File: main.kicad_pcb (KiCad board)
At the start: 2 copper layers, 221.6 x 89.6 mm, 122 parts, among them SW1 Kailh-Choc, SW10 Kailh-Choc, SW11 Kailh-Choc, SW12 Kailh-Choc, SW13 Kailh-Choc, SW14 Kailh-Choc, SW15 Kailh-Choc, SW16 Kailh-Choc, SW17 Kailh-Choc, SW18 Kailh-Choc, SW19 Kailh-Choc, SW2 Kailh-Choc, SW20 Kailh-Choc, SW21 Kailh-Choc, SW22 Kailh-Choc, SW23 Kailh-Choc, SW24 Kailh-Choc, SW25 Kailh-Choc, SW26 Kailh-Choc, SW27 Kailh-Choc, SW28 Kailh-Choc, SW29 Kailh-Choc, SW3 Kailh-Choc, SW30 Kailh-Choc, SW31 Kailh-Choc, SW32 Kailh-Choc, SW33 Kailh-Choc, SW34 Kailh-Choc, SW4 Kailh-Choc, SW5 Kailh-Choc, SW6 Kailh-Choc, SW7 Kailh-Choc, SW8 Kailh-Choc, SW9 Kailh-Choc, U1 nice_nano, U2 nice_nano

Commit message: Update PCB silk
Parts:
- removed kibuzzard-6361C7AA: G***, kibuzzard-6361C7AA
- added kibuzzard-63703FC3: G***, kibuzzard-63703FC3, B.Cu at (84.8, 87.8)

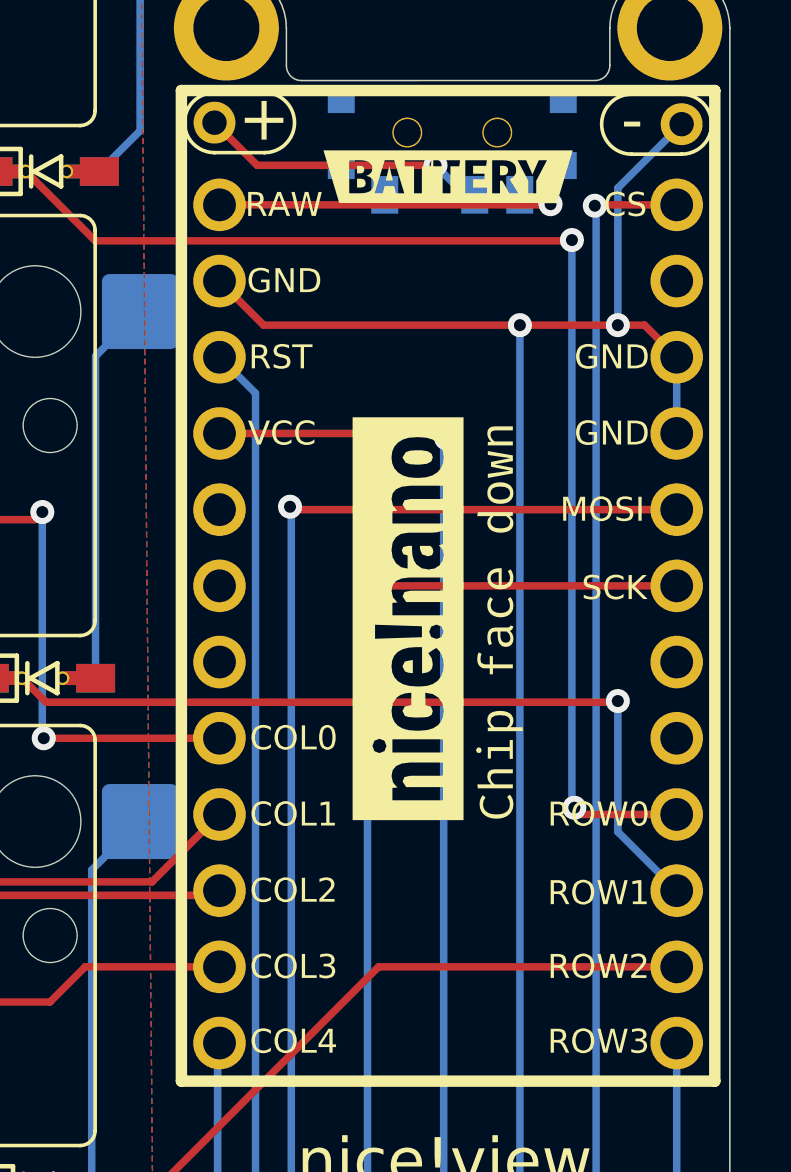
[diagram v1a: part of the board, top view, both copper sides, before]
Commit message: Use local library only
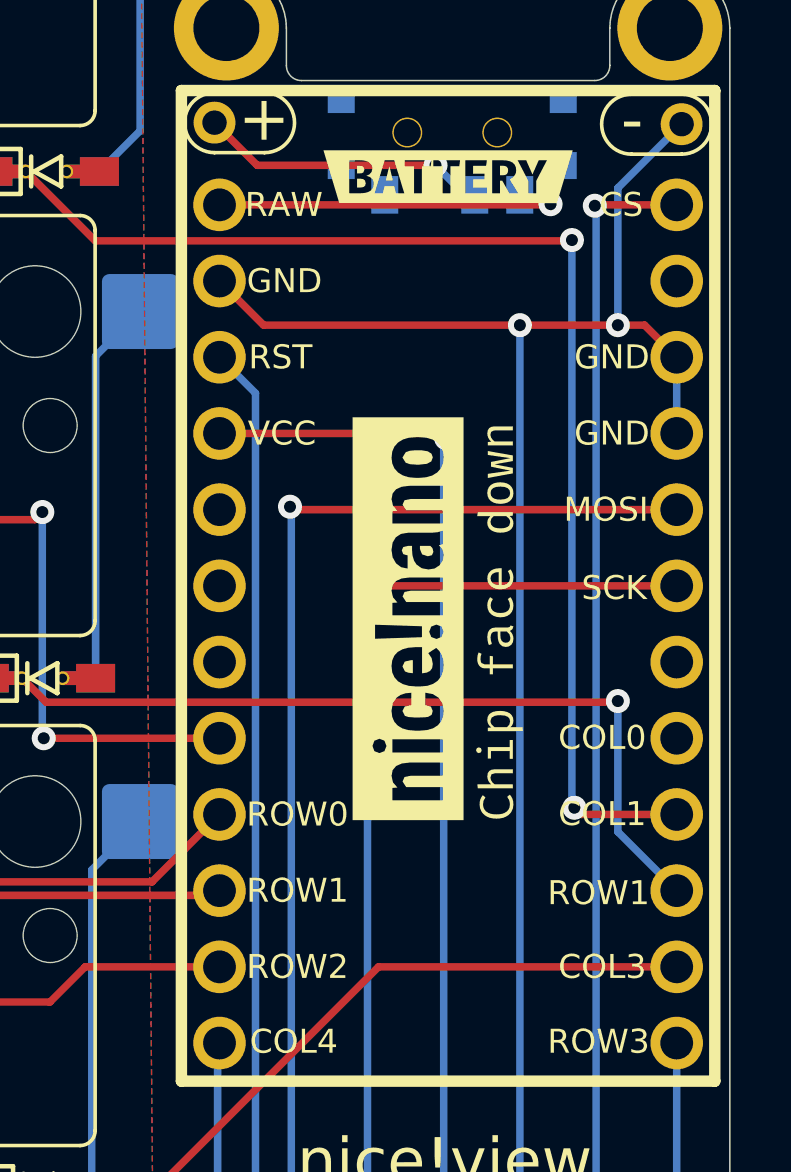
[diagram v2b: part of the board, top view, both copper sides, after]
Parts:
- Bat+0, Bat+1, BatGND0, BatGND1: footprint * duckyb-collection:1pin_Battery -> urchin-footprints:1pin_Battery
- D1, D10, D11, D12, D13, D14, D15, D16, D17, D18, D19, D2, D20, D21, D22, D23, D24, D25, D26, D27, D28, D29, D3, D30, D31, D32, D33, D34, D4, D5, D6, D7, D8, D9: footprint * duckyb-collection:SMD_Diode_Tiny -> urchin-footprints:SMD_Diode_Tiny
- Display1, Display2: footprint * duckyb-collection:nice_view -> urchin-footprints:nice_view
- REF_PUCK_R (x2): footprint * duckyb-collection:Tenting_Puck2_no_pads -> urchin-footprints:Tenting_Puck2_no_pads
- SW1, SW10, SW11, SW12, SW13, SW14, SW15, SW16, SW17, SW18, SW19, SW2, SW20, SW21, SW22, SW23, SW24, SW25, SW26, SW27, SW28, SW29, SW3, SW30, SW31, SW32, SW33, SW34, SW4, SW5, SW6, SW7, SW8, SW9: footprint * duckyb-collection:SW_Hotswap_Kailh_Choc_V1_tweaked -> urchin-footprints:SW_Hotswap_Kailh_Choc_V1_tweaked
- SW_POWER0, SW_POWER1: footprint * duckyb-collection:SPDT_C128955 -> urchin-footprints:smt-slider-switch
- U1, U2: footprint * duckyb-collection:nice_nano -> urchin-footprints:nice_nano
- mouse-bite-2mm-slot (x2): footprint Duckyb-Parts:mouse-bite-5mm-slot-with-space-for-track -> urchin-footprints:mouse-bite-5mm-slot-with-space-for-track
- turned REF_PUCK_R to -177 degrees

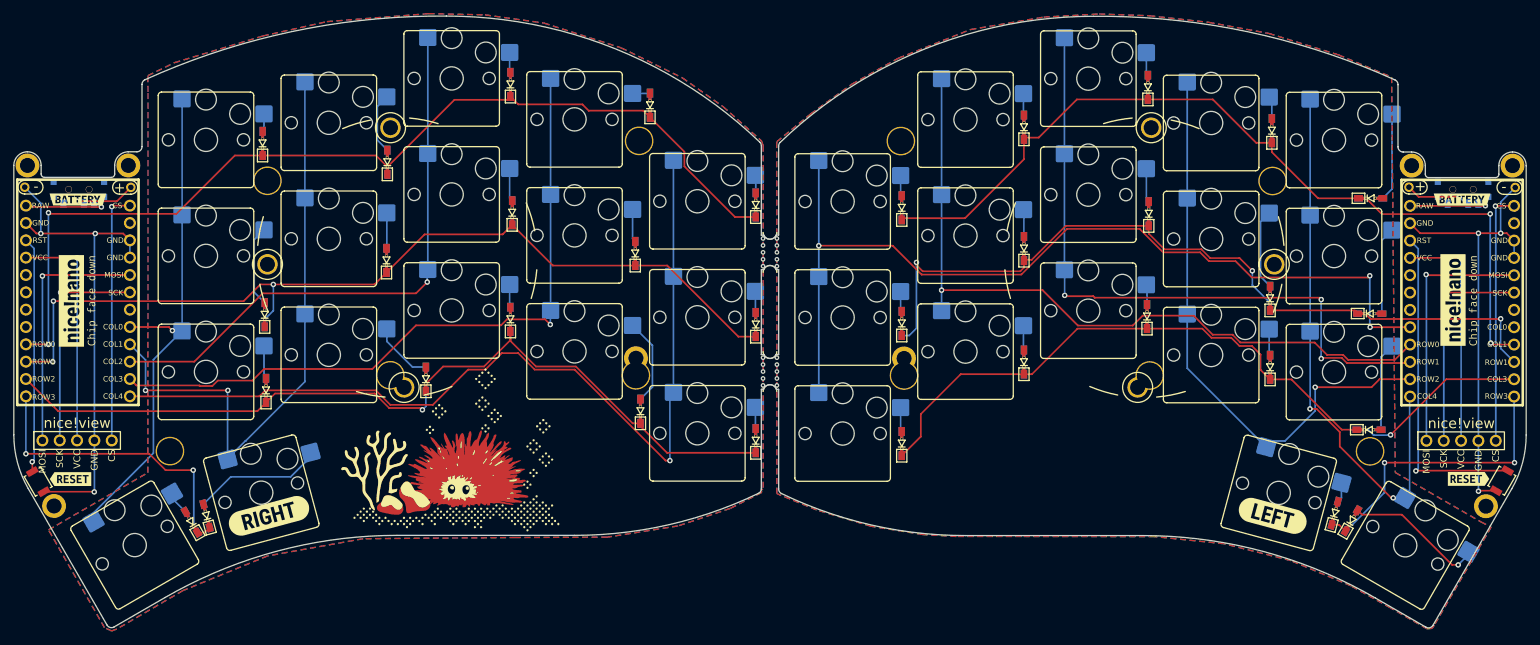
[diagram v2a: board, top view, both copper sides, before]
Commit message: Remove diode footprint from the top surface
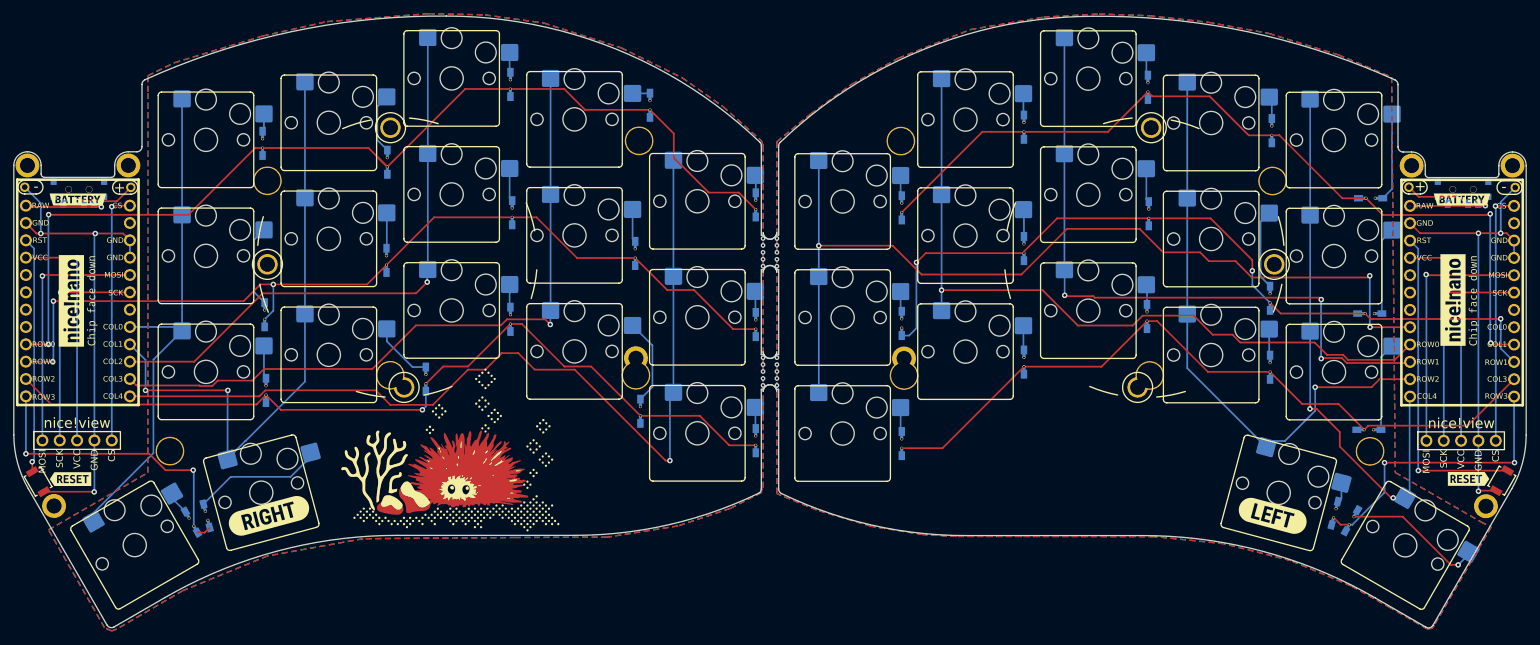
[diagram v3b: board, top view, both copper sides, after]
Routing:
- net R_ROW0: track 143.4 -> 147.6 mm
- net R_ROW2: track 125.7 -> 123.4 mm
- net ROW2: track 109.4 -> 107.1 mm, vias 1 -> 0
- net ROW1: track 115.1 -> 116.1 mm
- net ROW0: track 124.4 -> 123.5 mm
- net RESET: track 47.9 -> 47.3 mm
- net R_COL0: vias 1 -> 0
